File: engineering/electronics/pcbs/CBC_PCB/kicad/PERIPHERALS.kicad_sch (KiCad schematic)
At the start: 7 parts, among them J2 AT13-12PB-BM03

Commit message: fix: restore CBC schematic library nicknames
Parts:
- C25, C26: symbol CBC_PCB:CC0402KRX7R7BB104 -> EasyEDA_Lib:CC0402KRX7R7BB104
- J2: symbol CBC_PCB:AT13-12PB-BM03 -> 2026-04-30_07-21-07:AT13-12PB-BM03
- R10, R11: symbol CBC_PCB:RC0402FR-074K7L -> EasyEDA_Lib:RC0402FR-074K7L
- U1, U6: symbol CBC_PCB:DS18B20Z+T&amp;R -> EasyEDA_Lib:DS18B20Z+T&amp;R
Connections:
- net +3V3: now also C25.2, C26.2, R10.2, R11.2, U1.3 (VDD), U6.3 (VDD)
- net 12V_ISOLATED: now also J2.4, J2.5, J2.6
- net 12V_TRIGGER_SIG: now also J2.11
- net CANH_DRONE: now also J2.9
- net CANL_DRONE: now also J2.8
- net DATA1: now also R10.1, U1.4 (DQ)
- net DATA2: now also R11.1, U6.4 (DQ)
- net GND: now also C25.1, C26.1, J2.12, U1.5 (GND), U6.5 (GND)
- net GNDE: now also J2.1, J2.2, J2.3
- net GND_CB: now also J2.10
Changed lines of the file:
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@@
 	)
 	(symbol
-		(lib_id "CBC_PCB:CC0402KRX7R7BB104")
+		(lib_id "EasyEDA_Lib:CC0402KRX7R7BB104")
 		(at 68.58 171.45 90)
 		(unit 1)
@@
 	)
 	(symbol
-		(lib_id "CBC_PCB:DS18B20Z+T&amp;R")
+		(lib_id "EasyEDA_Lib:DS18B20Z+T&amp;R")
 		(at 38.1 165.1 0)
 		(mirror y)
@@
 	)
 	(symbol
-		(lib_id "CBC_PCB:RC0402FR-074K7L")
+		(lib_id "EasyEDA_Lib:RC0402FR-074K7L")
 		(at 55.88 133.35 90)
 		(unit 1)
@@
 	)
 	(symbol
-		(lib_id "CBC_PCB:DS18B20Z+T&amp;R")
+		(lib_id "EasyEDA_Lib:DS18B20Z+T&amp;R")
 		(at 36.83 134.62 0)
 		(mirror y)
@@
 	)
 	(symbol
-		(lib_id "CBC_PCB:RC0402FR-074K7L")
+		(lib_id "EasyEDA_Lib:RC0402FR-074K7L")
 		(at 57.15 163.83 90)
 		(unit 1)
@@
 	)
 	(symbol
-		(lib_id "CBC_PCB:CC0402KRX7R7BB104")
+		(lib_id "EasyEDA_Lib:CC0402KRX7R7BB104")
 		(at 67.31 140.97 90)
 		(unit 1)
@@
 	)
 	(symbol
-		(lib_id "CBC_PCB:AT13-12PB-BM03")
+		(lib_id "2026-04-30_07-21-07:AT13-12PB-BM03")
 		(at 31.75 38.1 0)
 		(unit 1)

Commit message: fix: qualify CBC connector footprint refs
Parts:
- J2: footprint CONN_AT13-12X-BMXX_AMP -> CBC_PCB:CONN_AT13-12X-BMXX_AMP
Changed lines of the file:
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@@
 			)
 		)
-		(property "Footprint" "CONN_AT13-12X-BMXX_AMP"
+		(property "Footprint" "CBC_PCB:CONN_AT13-12X-BMXX_AMP"
 			(at 31.75 38.1 0)
 			(hide yes)

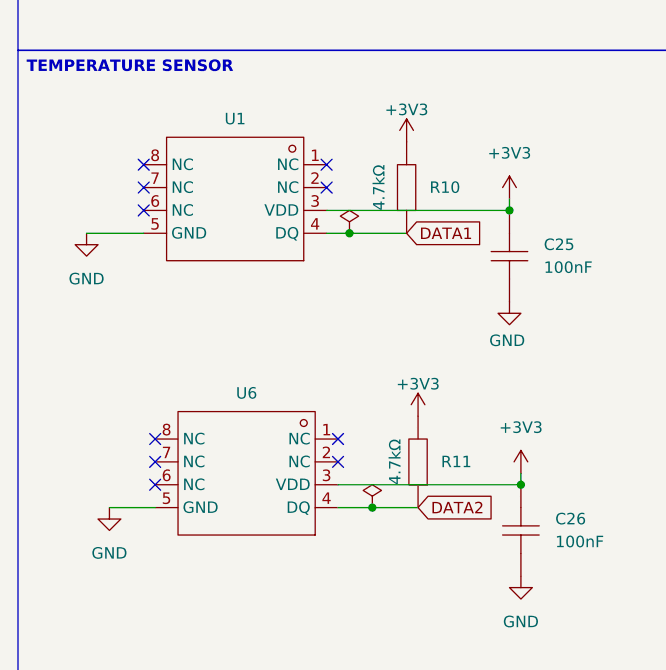
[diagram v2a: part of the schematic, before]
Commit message: fix: assign CBC imported symbol pin types
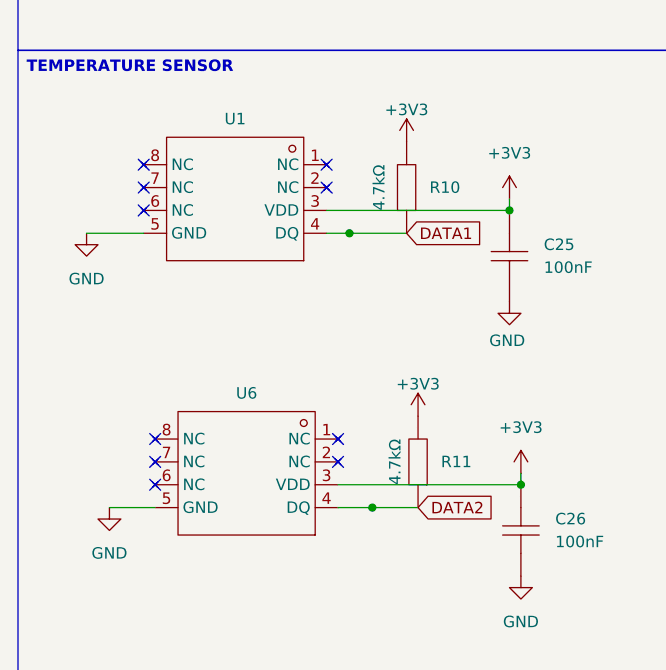
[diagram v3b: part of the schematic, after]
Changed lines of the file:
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@@
-	)
-	(symbol
-		(lib_id "power:PWR_FLAG")
-		(at 49.53 138.43 0)
-		(unit 1)
-		(body_style 1)
-		(exclude_from_sim no)
-		(in_bom yes)
-		(on_board yes)
-		(in_pos_files yes)
-		(dnp no)
-		(fields_autoplaced yes)
-		(property "Reference" "#FLG052"
-			(at 49.53 136.525 0)
-			(hide yes)
-			(show_name no)
-			(do_not_autoplace no)
-			(effects
-				(font
-					(size 1.27 1.27)
-				)
-			)
-		)
-		(property "Value" "PWR_FLAG"
-			(at 49.53 133.35 0)
-			(hide yes)
-			(show_name no)
-			(do_not_autoplace no)
-			(effects
-				(font
-					(size 1.27 1.27)
-				)
-			)
-		)
-		(property "Footprint" ""
-			(at 49.53 138.43 0)
-			(hide yes)
-			(show_name no)
-			(do_not_autoplace no)
-			(effects
-				(font
-					(size 1.27 1.27)
-				)
-			)
-		)
-		(property "Datasheet" ""
-			(at 49.53 138.43 0)
-			(hide yes)
-			(show_name no)
-			(do_not_autoplace no)
-			(effects
-				(font
-					(size 1.27 1.27)
-				)
-			)
-		)
-		(property "Description" "Special symbol for telling ERC where power comes from"
-			(at 49.53 138.43 0)
-			(hide yes)
-			(show_name no)
-			(do_not_autoplace no)
-			(effects
-				(font
-					(size 1.27 1.27)
-				)
-			)
-		)
-		(pin "1"
-		)
-		(instances
-			(project "CBC_PCB"
-				(path "/d195d1ee-585b-4211-912f-f5dd5687bc63/b4c95d27-7981-477f-a8ef-d2ce83f3675e"
-					(reference "#FLG052")
-					(unit 1)
-				)
-			)
-		)
 	)
 	(symbol
@@
 					(unit 1)
 				)
-			)
-		)
-	)
-	(symbol
-		(lib_id "power:PWR_FLAG")
-		(at 52.07 168.91 0)
-		(unit 1)
-		(body_style 1)
-		(exclude_from_sim no)
-		(in_bom yes)
-		(on_board yes)
-		(in_pos_files yes)
-		(dnp no)
-		(fields_autoplaced yes)
-		(property "Reference" "#FLG053"
-			(at 52.07 167.005 0)
-			(hide yes)
-			(show_name no)
-			(do_not_autoplace no)
-			(effects
-				(font
-					(size 1.27 1.27)
-				)
-			)
-		)
-		(property "Value" "PWR_FLAG"
-			(at 52.07 163.83 0)
-			(hide yes)
-			(show_name no)
-			(do_not_autoplace no)
-			(effects
-				(font
-					(size 1.27 1.27)
-				)
-			)
-		)
-		(property "Footprint" ""
-			(at 52.07 168.91 0)
-			(hide yes)
-			(show_name no)
-			(do_not_autoplace no)
-			(effects
-				(font
-					(size 1.27 1.27)
-				)
-			)
-		)
-		(property "Datasheet" ""
-			(at 52.07 168.91 0)
-			(hide yes)
-			(show_name no)
-			(do_not_autoplace no)
-			(effects
-				(font
-					(size 1.27 1.27)
-				)
-			)
-		)
-		(property "Description" "Special symbol for telling ERC where power comes from"
-			(at 52.07 168.91 0)
-			(hide yes)
-			(show_name no)
-			(do_not_autoplace no)
-			(effects
-				(font
-					(size 1.27 1.27)
-				)
-			)
-		)
-		(pin "1"
-		)
-		(instances
-			(project "CBC_PCB"
-				(path "/d195d1ee-585b-4211-912f-f5dd5687bc63/b4c95d27-7981-477f-a8ef-d2ce83f3675e"
-					(reference "#FLG053")
-					(unit 1)
-				)
